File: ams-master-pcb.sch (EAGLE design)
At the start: 172 parts, among them J1 M50-3601042, J2 TE-776087, Q1 STD45P4LLF6AG, Q2 BSS138, Q3 BSS138, Q4 BSS138, Q7 FQD3P50, Q8 FQD3P50, U1 MCP2562FD, U12 RM46L852CPGET, U16 LM3671MF-3.3/NOPB, U17 SN74LVC1G02DBV, U18 LM3671MF-1.2/NOPB, U2 SN74LVC1G32DBV, U22 FAN3214, U23 FAN3214, U24 CSD17506Q5A, U25 CSD17506Q5A, U26 SN74ALVC125DR, U27 CSD17506Q5A, U3 SN74LVC1G08DBV, U30 ISO7221, U31 ISO7221, U32 PDS1-S5-S5-M-TR, U33 ISO7221, U34 ISO7221, U35 PDS1-S5-S5-M-TR, U36 ADC121S021, U37 ADC121S021, U42 TPS54540DDARQ1, U5 CD4050BD, U6 CD4050BD, U7 MCP2562FD, U9 CD4050BD, Y2 16MHz

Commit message: Started updating TS sections, moved SPI stuff. Needs to look a lot nicer still.
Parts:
- removed JP14, JP15, JP27, JP28, JP29, JP30, JP32, JP33, JP34, JP35: (no value), pinhead:PINHD-1X1
- removed JP16, JP17, JP22: 0R, FormE:TWO-WAY-JUMPER-0603
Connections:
- removed net N$26: JP22.P$1, U26B.IN
- removed net N$27: JP16.P$2, JP34.1, U33.INA
- removed net N$54: JP17.P$2, JP35.1, U34.INA
- removed net OPT_BATTERY_VOLTAGE_MONITOR_CS: JP16.P$3
- removed net OPT_BATTERY_VOLTAGE_MONITOR_MISO: JP22.P$3
- removed net OPT_BATTERY_VOLTAGE_MONITOR_SCK: JP17.P$3
- new net N$3: U26B.IN
- new net N$8: R85.2, U26B.!OE!
- net BATTERY_VOLTAGE_IS_AVAILABLE: no longer JP30.1
- net BATTERY_VOLTAGE_MISO: no longer JP22.P$2, JP29.1
- net BATTERY_VOLTAGE_MONITOR_CS: now also U33.INA; no longer JP14.1, JP16.P$1, R85.2, U26B.!OE!
- net VEHICLE_VOLTAGE_IS_AVAILABLE: no longer JP28.1
- net VEHICLE_VOLTAGE_MISO: no longer JP27.1
- net VEHICLE_VOLTAGE_MONITOR_CS: no longer JP32.1
- net VOLTAGE_MONITOR_MISO: no longer JP15.1
- net VOLTAGE_MONITOR_SCLK: now also U34.INA; no longer JP17.P$1, JP33.1
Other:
- note removed: "TEST POINTS FOR HV MEASURING ADC"
- moved on the sheet: C3, C4, C75, C76, C79, C81, C87, C88, C91, C93, D18, D19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

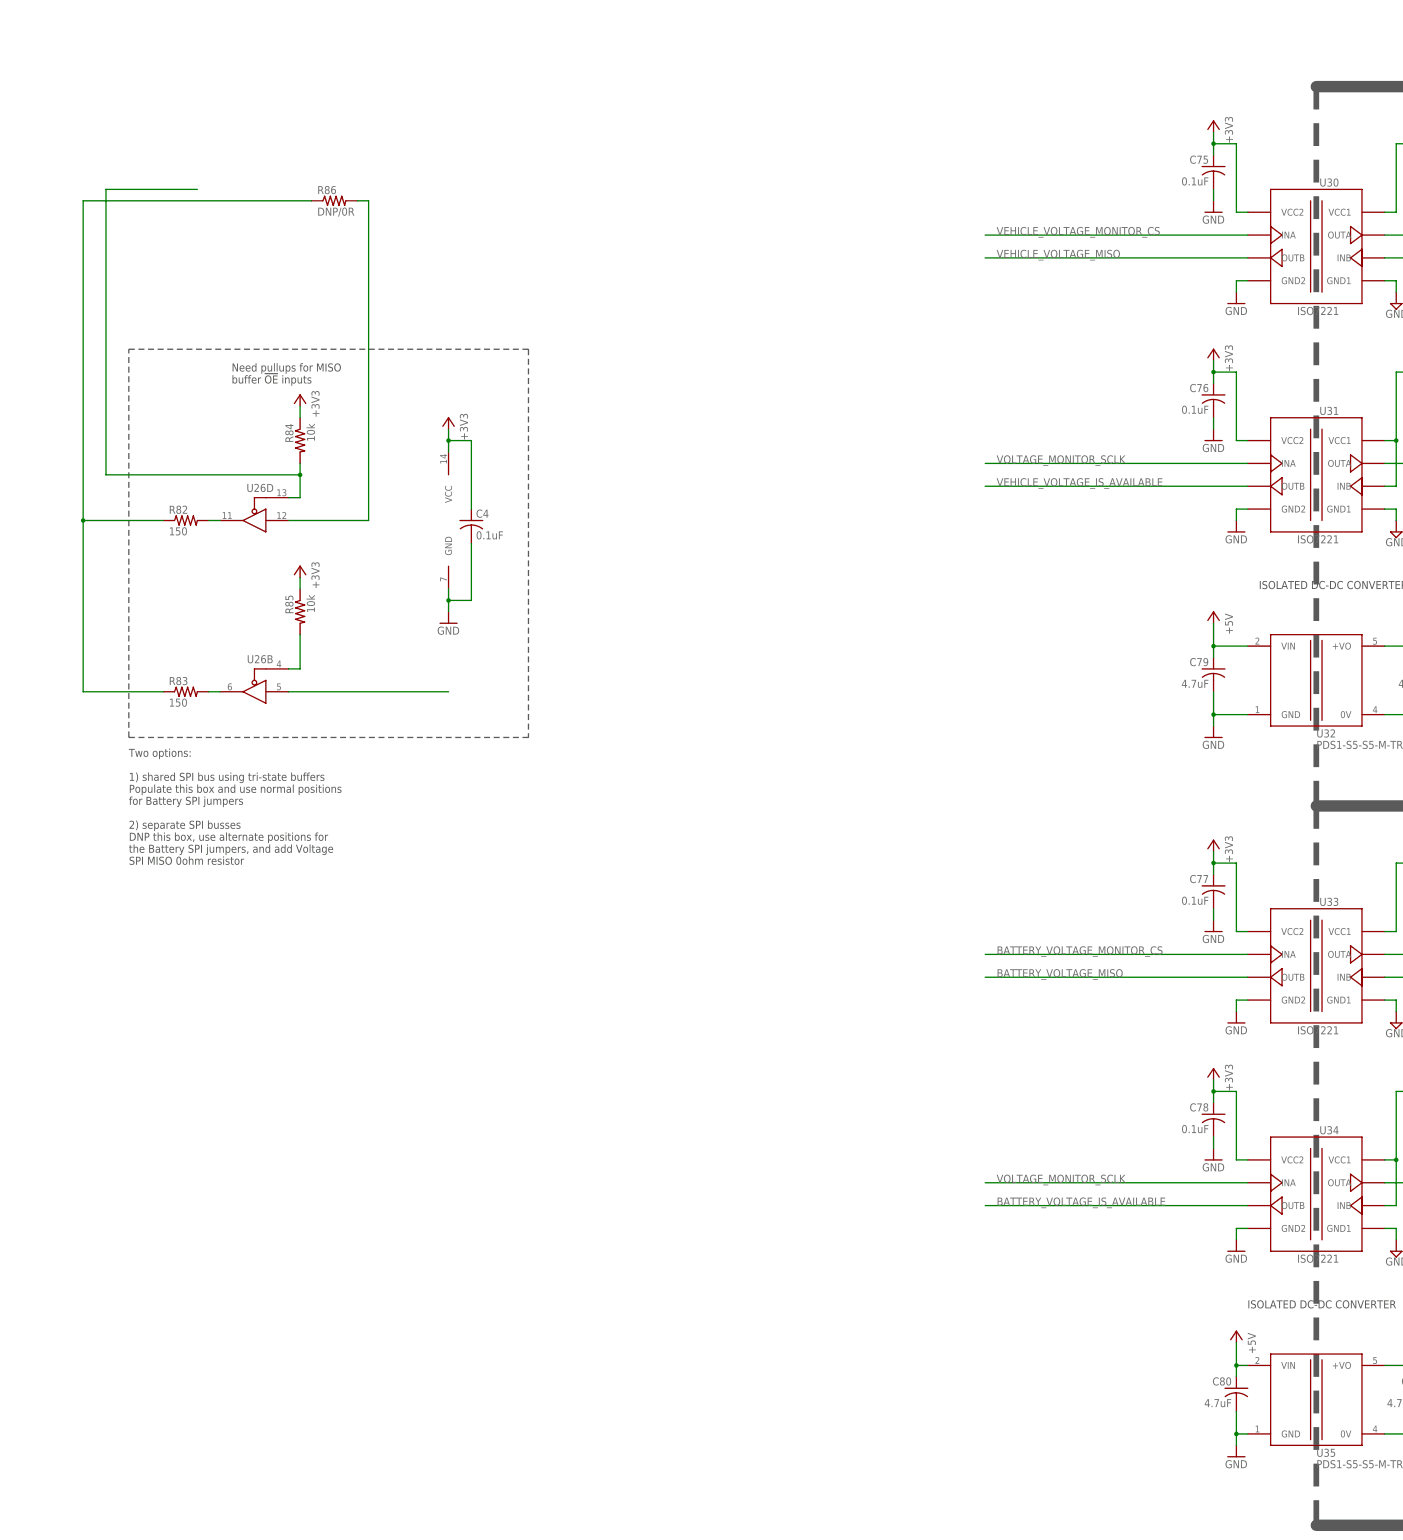
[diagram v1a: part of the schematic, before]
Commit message: Changed a bit of the Isolated Portion
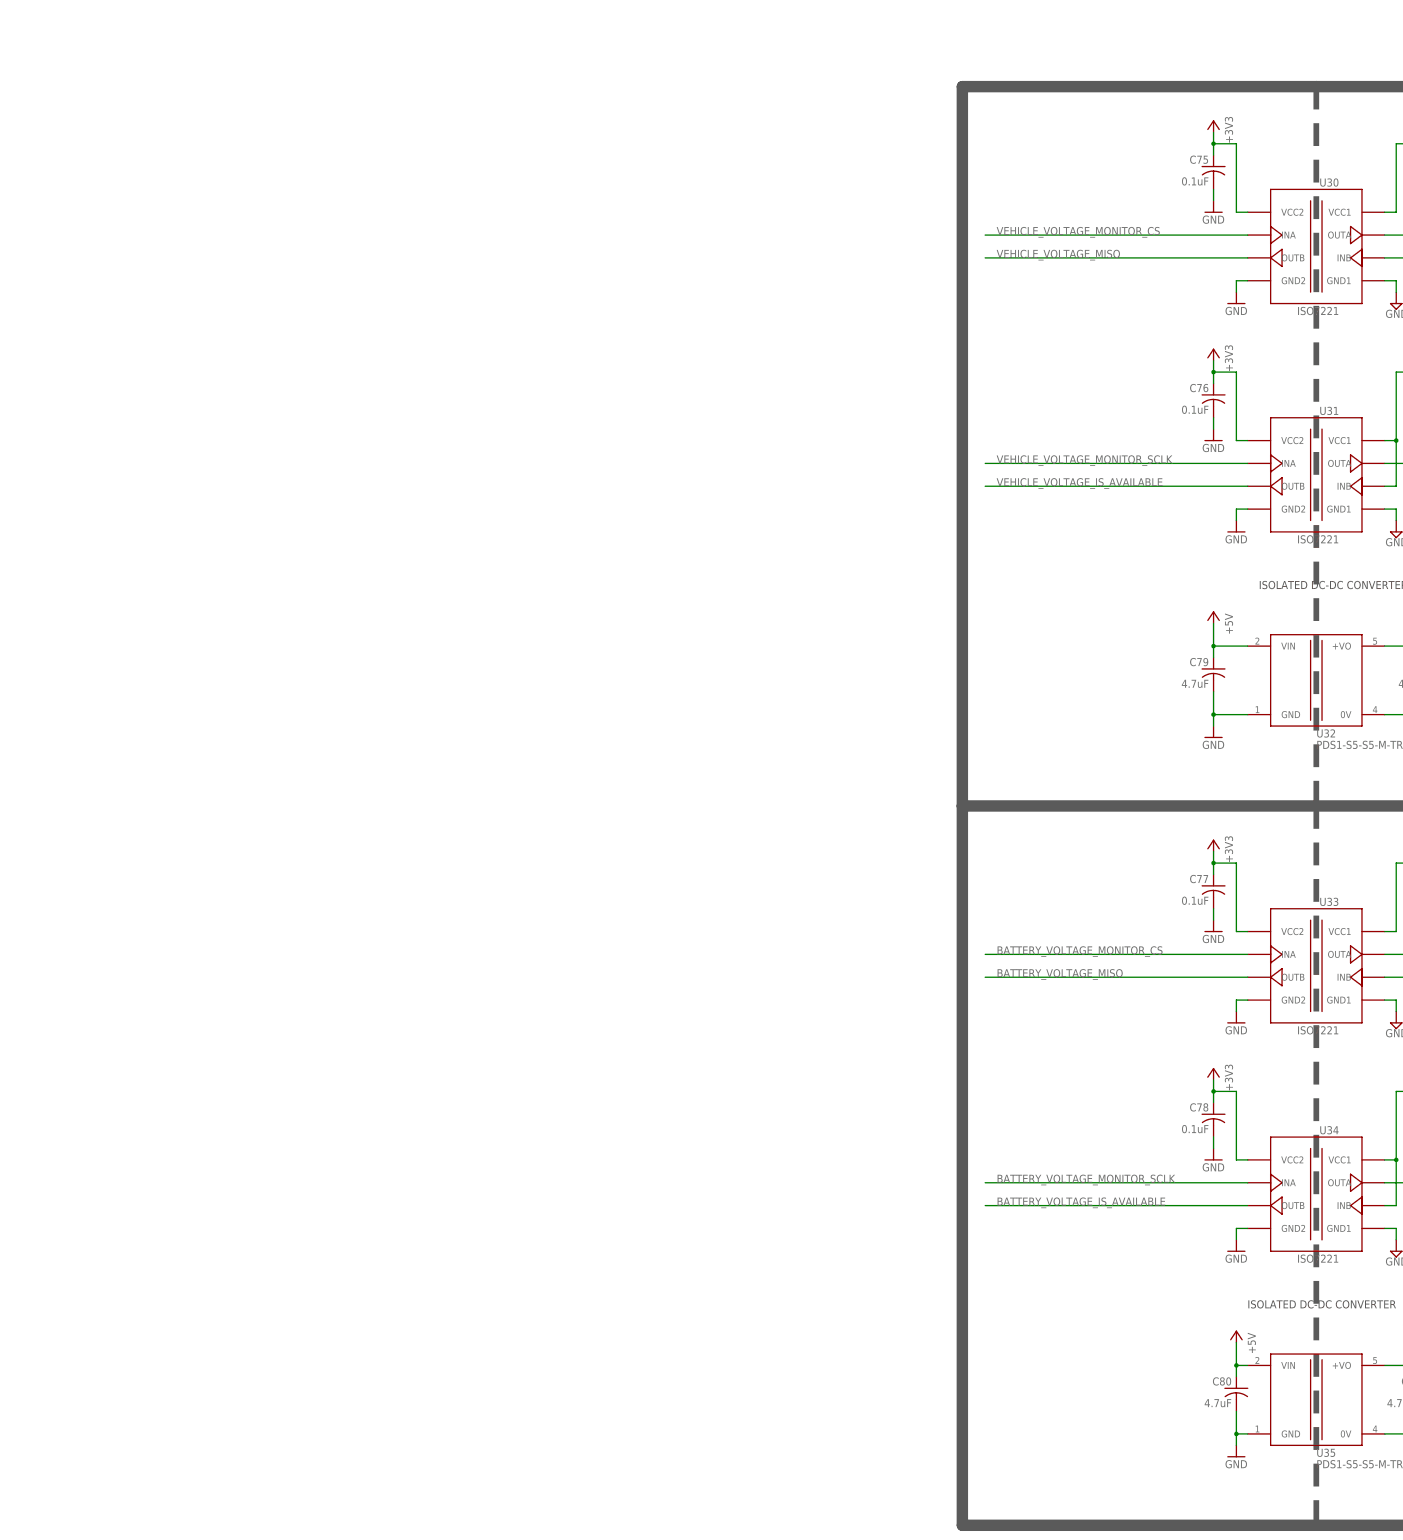
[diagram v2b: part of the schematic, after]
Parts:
- removed C4: 0.1uF, rcl:C-USC0603K
- removed R82, R83: 150, rcl:R-US_R0603
- removed R84, R85: 10k, rcl:R-US_R0603
- removed R86: DNP/0R, rcl:R-US_R0603
- removed U26: SN74ALVC125DR, FormE:SN74ALVC125DR
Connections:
- removed net N$3: U26B.IN
- removed net N$48: R83.2, U26B.OUT
- removed net N$52: R82.2, U26D.OUT
- removed net N$8: R85.2, U26B.!OE!
- removed net VOLTAGE_MONITOR_MISO: R82.1, R83.1, R86.1
- removed net VOLTAGE_MONITOR_SCLK: U31.INA, U34.INA
- new net BATTERY_VOLTAGE_MONITOR_SCLK: U34.INA
- new net VEHICLE_VOLTAGE_MONITOR_SCLK: U31.INA
- net +3V3: no longer C4.1, R84.1, R85.1, U26G$4.VCC
- net GND: no longer C4.2, U26G$4.GND
- net VEHICLE_VOLTAGE_MISO: no longer R86.2, U26D.IN
- net VEHICLE_VOLTAGE_MONITOR_CS: no longer R84.2, U26D.!OE!
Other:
- note removed: "Need pullups for MISO buffer !OE! inputs"
- note removed: "Two options: 1) shared SPI bus using tri-state buffers Populate this box and use normal positions for Battery SPI jumpers 2) separate SPI busses DNP this box, use alternate positions for the Battery SPI jumpers, and add Voltage SPI MISO 0ohm resistor"

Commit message: Adding Connections to Hercules
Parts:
- added 5V/1, 5V/2, LED1: GREEN, FormE:LEDCHIP-LED0805
- added R3, R30, R6: 1k, rcl:R-US_R0603
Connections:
- removed net BATTERY_VOLTAGE_MISO: U33.OUTB
- new net BATTERY_VOLTAGE_MONITOR_MISO: U12IO.N2HET1[5]/SPI4SOMI[0]/N2HET2[12]/EPWM3B, U33.OUTB
- new net N$3: 5V/2.C, R3.2
- new net N$46: LED1.C, R30.2
- new net N$8: 5V/1.C, R6.2
- net +5V: now also LED1.A
- net +5V/1: now also 5V/1.A
- net +5V/2: now also 5V/2.A
- net BATTERY_VOLTAGE_MONITOR_CS: now also U12IO.N2HET1[3]/SPI4NCS[0]/USB2.SPEED/USB_FUNC.PUENON/N2HET2[10]/EQEP2B
- net BATTERY_VOLTAGE_MONITOR_SCLK: now also U12IO.N2HET1[0]/SPI4CLK/EPWM2B
- net GND: now also R30.1
- net GND2: now also R6.1
- net GND3: now also R3.1
- net IMD_PWM_OUT_3V3: now also U12IO.N2HET1[2]/SPI4SIMO[0]/EPWM3A
- net SC_FROM_OUTSIDE_SENSE: now also U12IO.N2HET1[4]/EPWM4B
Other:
- note added: "Make sure these are 400v components"
- note removed: "ADD LEDs SOURCE 400v components"
- moved on the sheet: C31, C32, L4

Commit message: Pinout on Hercules complete
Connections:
- removed net IRQ_AMS_GLV: U12IO.GIOA[0]/USB2.VP/USB_FUNC.RXDPI
- removed net RTC_!RST!: U12IO.GIOB[3]/USB2.RCV/USB_FUNC.RXDI
- removed net RTC_SQW: U12IO.GIOB[2]
- removed net VEHICLE_VOLTAGE_MISO: U30.OUTB
- new net CURRENT_SENSE_-750A_TO_+750A: U12IO.AD1IN[1]
- new net CURRENT_SENSE_-75A_TO_+75A: U12IO.AD1IN[0]
- new net INDICATOR_1: U12IO.N2HET1[14]/USB1.TXSE0
- new net INDICATOR_2: U12IO.N2HET1[30]/MII_RX_DV/USB1.SPEED/EQEP2S
- new net VEHICLE_VOLTAGE_MONITOR_MISO: U12IO.MIBSPI1SOMI[0], U30.OUTB
- net BATTERY_VOLTAGE_IS_AVAILABLE: now also U12IO.MIBSPI3SIMO[0]/AWM1_EXT_SEL[0]/ECAP3
- net BATTERY_VOLTAGE_MONITOR_CS: now also U12IO.MIBSPI3NCS[0]/AD2EVT/GIOB[2]/EQEP1I/N2HET2_PIN_NDIS; no longer U12IO.N2HET1[3]/SPI4NCS[0]/USB2.SPEED/USB_FUNC.PUENON/N2HET2[10]/EQEP2B
- net BATTERY_VOLTAGE_MONITOR_MISO: now also U12IO.MIBSPI3SOMI[0]/AWM1_EXT_ENA/ECAP2; no longer U12IO.N2HET1[5]/SPI4SOMI[0]/N2HET2[12]/EPWM3B
- net BATTERY_VOLTAGE_MONITOR_SCLK: now also U12IO.MIBSPI3CLK/AWM1_EXT_SEL[1]/EQEP1A; no longer U12IO.N2HET1[0]/SPI4CLK/EPWM2B
- net CONTACTOR_CLOSED_3V3: now also U12IO.GIOA[7]/N2HET2[6]/EPWM2A
- net CONTACTOR_OPEN_3V3: now also U12IO.GIOA[6]/N2HET2[4]/EPWM1B
- net FAULT_AMS_INDICATOR: now also U12IO.GIOB[0]/USB1.TXDAT
- net NEGATIVE_CONTACTOR_CTRL: now also U12IO.N2HET1[18]/EPWM6A
- net POSITIVE_CONTACTOR_CTRL: now also U12IO.N2HET1[20]/EPWM6B
- net PRECHARGE_CONTACTOR_CTRL: now also U12IO.N2HET1[16]/EPWM1SYNCI/EPWM1SYNCO
- net SC_AFTER_INTERCONNECT_SENSE: now also U12IO.MIBSPI3NCS[1]/N2HET1[25]/MDCLK
- net VEHICLE_VOLTAGE_IS_AVAILABLE: now also U12IO.MIBSPI1SIMO[0]
- net VEHICLE_VOLTAGE_MONITOR_CS: now also U12IO.MIBSPI1NCS[0]/MIBSPI1SOMI[1]/MII_TXD[2]/USB1.RCV/ECAP6
- net VEHICLE_VOLTAGE_MONITOR_SCLK: now also U12IO.MIBSPI1CLK
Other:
- note added: "NEEDS TO BE ISOLATED!!!"
- moved on the sheet: 5V/1, 5V/2, C1, C2, C3, C31, C32, C5, C50, C51, C52, C64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
